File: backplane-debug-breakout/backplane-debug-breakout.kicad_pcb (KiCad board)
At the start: 2 copper layers, 65 x 50.5 mm, 11 parts, among them J1 Conn_02x08_Odd_Even, J2 Conn_01x04, J3 Conn_01x01_Socket, J4 Conn_01x01_Socket, J5 Conn_01x04, SW2 SW_Omron_B3FS, SW3 EG1218, U1 UMFT234XF

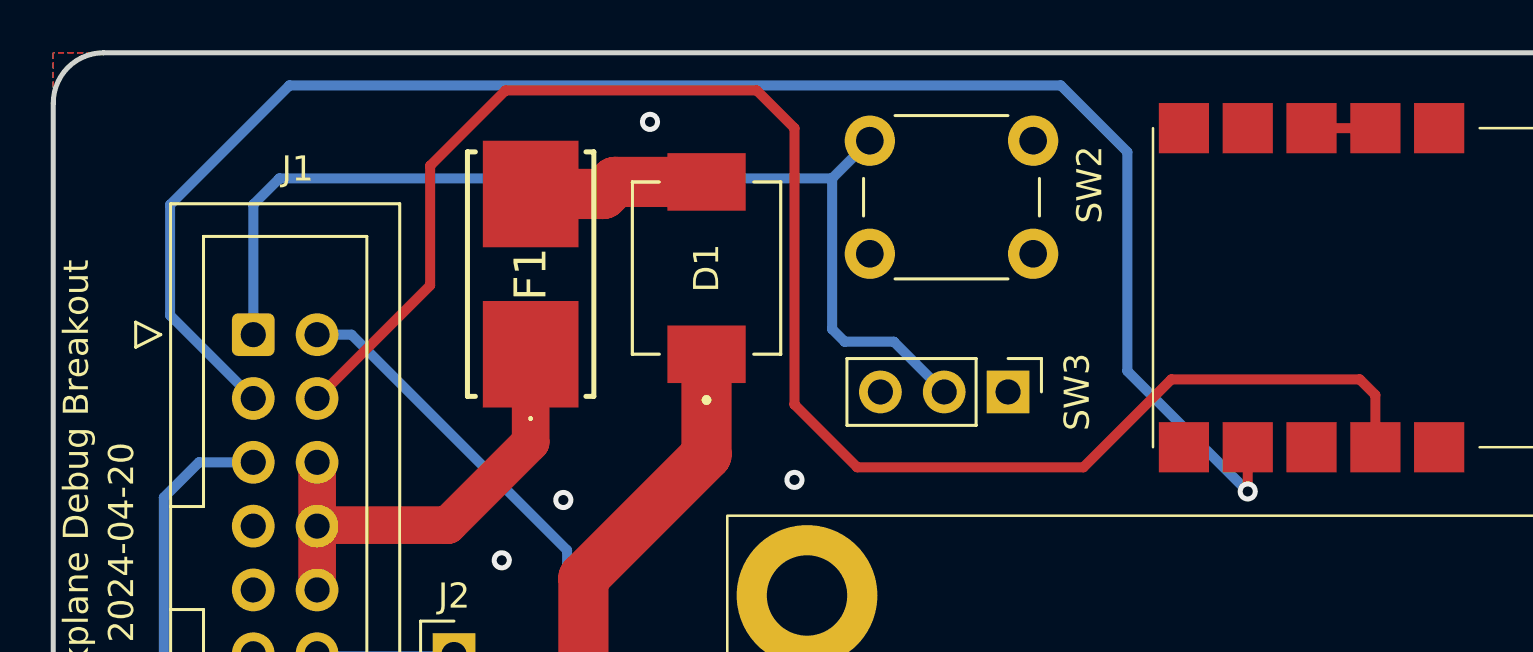
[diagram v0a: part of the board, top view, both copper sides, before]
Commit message: fixed tx-rx connections
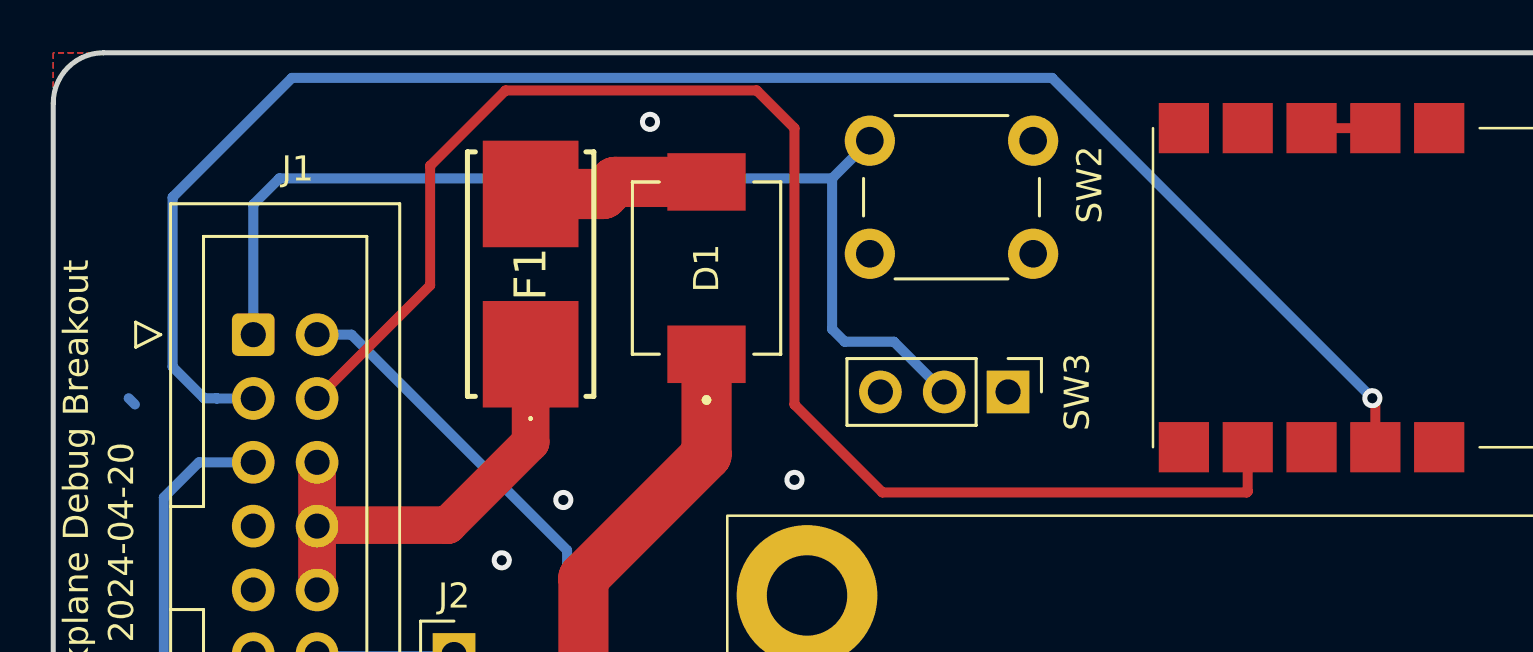
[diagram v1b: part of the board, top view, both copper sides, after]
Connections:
- U1 pad P7: /C3-UART-TX -> /C3-UART-RX
- U1 pad P9: /C3-UART-RX -> /C3-UART-TX
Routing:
- net /C3-UART-RX: track 66.4 -> 59.8 mm
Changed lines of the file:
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@@
 			)
 		)
-		(attr exclude_from_pos_files exclude_from_bom)
+		(attr exclude_from_pos_files exclude_from_bom allow_missing_courtyard)
 		(fp_rect
 			(start -3.175 -3.175)
@@
 			(size 2 2)
 			(layers "F.Cu" "F.Paste" "F.Mask")
-			(net 5 "/C3-UART-TX")
+			(net 8 "/C3-UART-RX")
 			(pinfunction "TXD")
 			(pintype "output")
@@
 			(size 2 2)
 			(layers "F.Cu" "F.Paste" "F.Mask")
-			(net 8 "/C3-UART-RX")
+			(net 5 "/C3-UART-TX")
 			(pinfunction "RXD")
 			(pintype "input")
@@
 			)
 		)
-		(property "Description" "16-position cable assembly socket"
+		(property "Description" "CONN HEADER VERT 16POS 2.54MM Y - 0"
 			(at 0 0 0)
 			(unlocked yes)
@@
 			)
 		)
-		(property "DPN" "H3DDH-1611618G-ND"
+		(property "DPN" "732-2095-ND"
 			(at 0 0 0)
 			(unlocked yes)
@@
 			)
 		)
-		(property "MPN" "H3DDH-161618G"
+		(property "MPN" "61201621621"
 			(at 0 0 0)
 			(unlocked yes)
@@
 			)
 		)
-		(property "MFR" "Assman"
+		(property "MFR" "Würth Elektronik"
 			(at 0 0 0)
 			(unlocked yes)
@@
 	)
 	(segment
-		(start 144.54 74.7)
-		(end 144.54 76.46)
+		(start 149.62 74.7)
+		(end 149.62 72.87)
 		(width 0.4)
 		(layer "F.Cu")
 		(net 5)
 	)
+	(segment
+		(start 149.62 72.87)
+		(end 149.5 72.75)
+		(width 0.4)
+		(layer "F.Cu")
+		(net 5)
+	)
 	(via
-		(at 144.54 76.46)
+		(at 149.5 72.75)
 		(size 0.8)
 		(drill 0.4)
@@
 	)
 	(segment
-		(start 139.75 62.95)
-		(end 137.1 60.3)
+		(start 101.75 71.5)
+		(end 103 72.75)
 		(width 0.4)
 		(layer "B.Cu")
@@
 	)
 	(segment
-		(start 144.54 76.46)
-		(end 139.75 71.67)
+		(start 103 72.75)
+		(end 103.5 72.75)
 		(width 0.4)
 		(layer "B.Cu")
@@
 	)
 	(segment
-		(start 139.75 71.67)
-		(end 139.75 62.95)
+		(start 101.75 64.75)
+		(end 101.75 71.5)
 		(width 0.4)
 		(layer "B.Cu")
@@
 	)
 	(segment
-		(start 101.65 65.05)
-		(end 101.65 69.45)
+		(start 136.75 60)
+		(end 106.5 60)
 		(width 0.4)
 		(layer "B.Cu")
@@
 	)
 	(segment
-		(start 101.65 69.45)
+		(start 100 72.75)
+		(end 100.25 73)
+		(width 0.4)
+		(layer "B.Cu")
+		(net 5)
+	)
+	(segment
+		(start 103.51 72.76)
 		(end 104.96 72.76)
 		(width 0.4)
@@
 	)
 	(segment
-		(start 106.4 60.3)
-		(end 101.65 65.05)
+		(start 106.5 60)
+		(end 101.75 64.75)
 		(width 0.4)
 		(layer "B.Cu")
@@
 	)
 	(segment
-		(start 137.1 60.3)
-		(end 106.4 60.3)
+		(start 103.5 72.75)
+		(end 103.51 72.76)
+		(width 0.4)
+		(layer "B.Cu")
+		(net 5)
+	)
+	(segment
+		(start 149.5 72.75)
+		(end 136.75 60)
 		(width 0.4)
 		(layer "B.Cu")
@@
 	)
 	(segment
-		(start 149.62 74.7)
-		(end 149.62 72.62)
+		(start 144.5 76.5)
+		(end 130 76.5)
 		(width 0.4)
 		(layer "F.Cu")
@@
 	)
 	(segment
-		(start 149 72)
-		(end 141.5 72)
+		(start 144.54 76.46)
+		(end 144.5 76.5)
 		(width 0.4)
 		(layer "F.Cu")
@@
 	)
 	(segment
-		(start 129 75.5)
+		(start 130 76.5)
 		(end 126.5 73)
+		(width 0.4)
+		(layer "F.Cu")
+		(net 8)
+	)
+	(segment
+		(start 112 68.26)
+		(end 107.5 72.76)
 		(width 0.4)
 		(layer "F.Cu")
@@
 	)
 	(segment
+		(start 125 60.5)
+		(end 115 60.5)
+		(width 0.4)
+		(layer "F.Cu")
+		(net 8)
+	)
+	(segment
+		(start 115 60.5)
+		(end 112 63.5)
+		(width 0.4)
+		(layer "F.Cu")
+		(net 8)
+	)
+	(segment
+		(start 144.54 74.7)
+		(end 144.54 76.46)
+		(width 0.4)
+		(layer "F.Cu")
+		(net 8)
+	)
+	(segment
 		(start 126.5 62)
 		(end 125 60.5)
 		(width 0.4)
 		(layer "F.Cu")
-		(net 8)
-	)
-	(segment
-		(start 115 60.5)
-		(end 112 63.5)
-		(width 0.4)
-		(layer "F.Cu")
-		(net 8)
-	)
-	(segment
-		(start 149.62 72.62)
-		(end 149 72)
-		(width 0.4)
-		(layer "F.Cu")
-		(net 8)
-	)
-	(segment
-		(start 125 60.5)
-		(end 115 60.5)
-		(width 0.4)
-		(layer "F.Cu")
-		(net 8)
-	)
-	(segment
-		(start 138 75.5)
-		(end 129 75.5)
-		(width 0.4)
-		(layer "F.Cu")
-		(net 8)
-	)
-	(segment
-		(start 112 68.26)
-		(end 107.5 72.76)
-		(width 0.4)
-		(layer "F.Cu")
-		(net 8)
-	)
-	(segment
-		(start 141.5 72)
-		(end 138 75.5)
-		(width 0.4)
-		(layer "F.Cu")

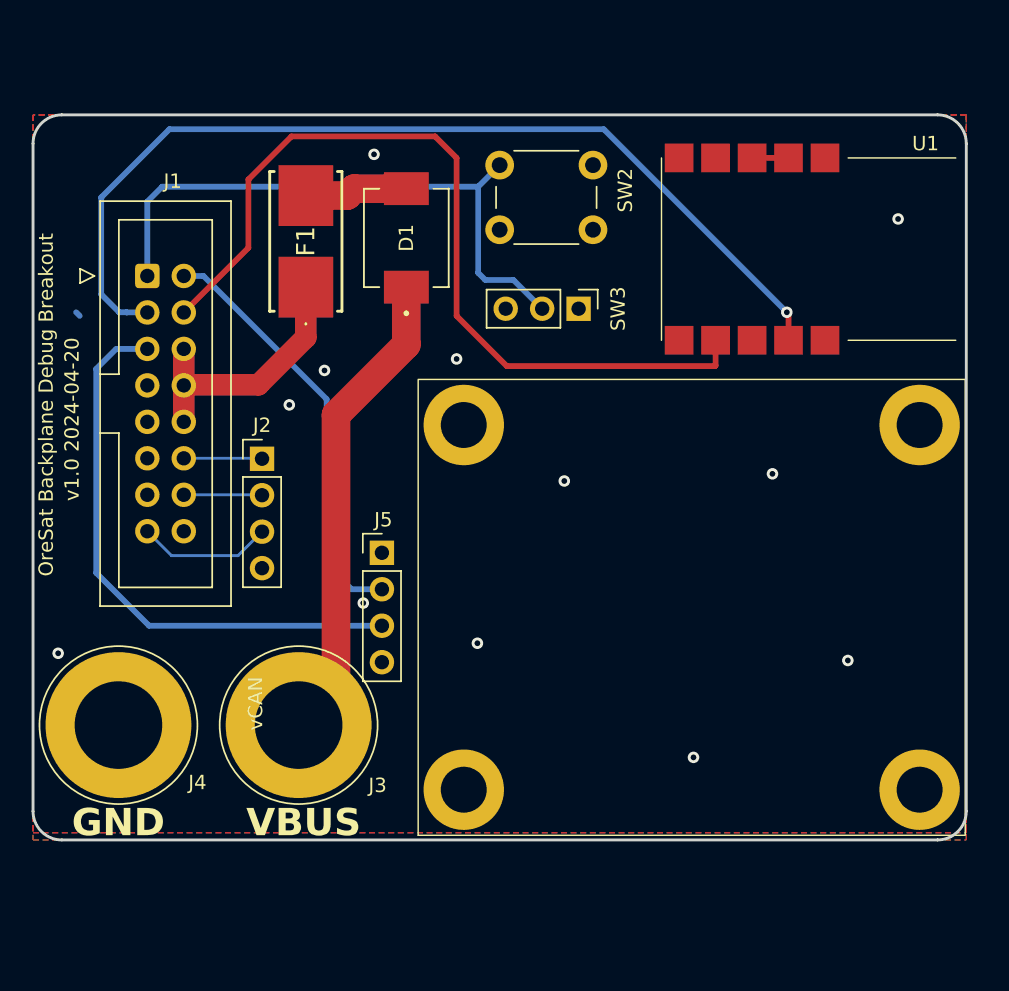
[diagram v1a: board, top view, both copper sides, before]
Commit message: added usb-serial connector to schematic and pcb
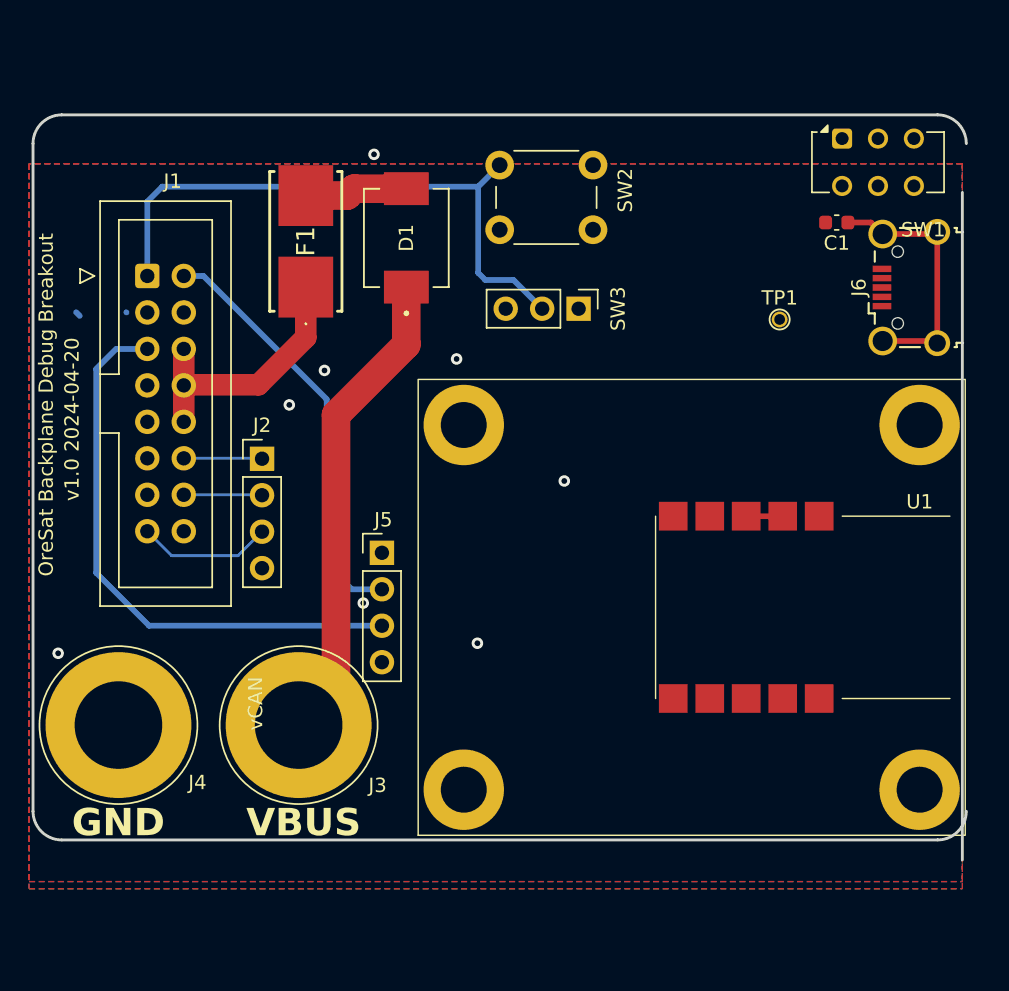
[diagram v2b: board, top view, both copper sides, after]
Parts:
- added C1: 100n, Capacitor_SMD:C_0603_1608Metric, F.Cu at (153.0, 66.5)
- added J6: 629105150521, Connector_USB:USB_Micro-B_Wuerth_629105150521_CircularHoles, F.Cu at (158.0, 71.0)
- added SW1: SW_Push_DPDT, oresat-passives:DPDT slide switch 6 pin, F.Cu at (159.0, 67.5)
- added TP1: TestPoint, oresat-misc:TestPoint-0.75mm-th, F.Cu at (149.0, 73.2)
- moved U1 25.0 mm to (161.4, 87.0)
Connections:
- U1 pad P7: /C3-UART-RX -> Net-(U1-TXD)
- U1 pad P9: /C3-UART-TX -> Net-(U1-RXD)
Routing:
- net /C3-UART-TX: track 67.8 -> 0.37 mm, vias 1 -> 0
- net /C3-UART-RX: track 59.8 -> 0.00 mm
- net Net-(J6-Shield): track 0.00 -> 18.4 mm
- net GND: vias 12 -> 8
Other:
- board size 65 x 50.5 mm -> 65 x 51.9 mm

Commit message: made changes to layout of pcb
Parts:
- removed J3: Conn_01x01_Socket, Connector:Banana_Jack_1Pin
- J4: value Conn_01x01_Socket -> Conn_01x02_Socket; footprint Connector:Banana_Jack_1Pin -> oresat-connectors:PHOENIX_1995499
- moved SW3 16.5 mm to (122.3, 62.0)
- moved F1 14.3 mm to (130.3, 67.6)
- moved D1 13.8 mm to (136.8, 67.6)
- moved SW2 13.5 mm to (123.0, 70.8)
- moved SW1 9.85 mm to (149.3, 69.2)
- moved J4 9.15 mm to (97.0, 94.5)
- moved TP1 4.50 mm to (152.4, 70.3)
- moved J6 3.15 mm to (158.1, 67.9)
- moved U1 2.71 mm to (161.1, 84.2)
- moved vCAN 2.71 mm to (126.8, 103.3)
- moved C1 2.40 mm to (152.9, 64.1)
- moved J2 2.30 mm to (115.0, 81.9)
- moved J1 1.78 mm to (106.7, 70.6)
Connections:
- J4 pad 1: GND -> Net-(D1-A)
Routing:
- net /C3-UART-TX: track 0.37 -> 53.2 mm
- net Net-(U1-RXD): track 0.26 -> 49.2 mm
- net /C3-UART-RX: track 0.00 -> 42.9 mm, vias 0 -> 1
- net Net-(U1-TXD): track 0.00 -> 35.0 mm
- net /SD: track 42.3 -> 25.2 mm
- net Net-(J6-D-): track 0.00 -> 11.5 mm
- net /VBUS: track 18.5 -> 29.2 mm
- net Net-(D1-A): track 34.3 -> 44.2 mm
- net Net-(J6-D+): track 0.00 -> 9.10 mm, vias 0 -> 2
- net Net-(J6-VBUS): track 0.00 -> 4.22 mm
- net /CAN_L: track 29.6 -> 27.7 mm
- net /CAN_H: track 39.8 -> 38.1 mm
- net /OPD_SCL: track 9.87 -> 11.5 mm
- net /OPD_PWR: track 5.46 -> 6.35 mm
- net /OPD_SDA: track 5.46 -> 6.34 mm
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- added copper zone on B.Cu, net Net-(D1-A)
- added copper zone on F.Cu, net Net-(D1-A)
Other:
- board size 65 x 51.9 mm -> 65 x 60.5 mm
- board text removed: "GND"
- board text removed: "VBUS"

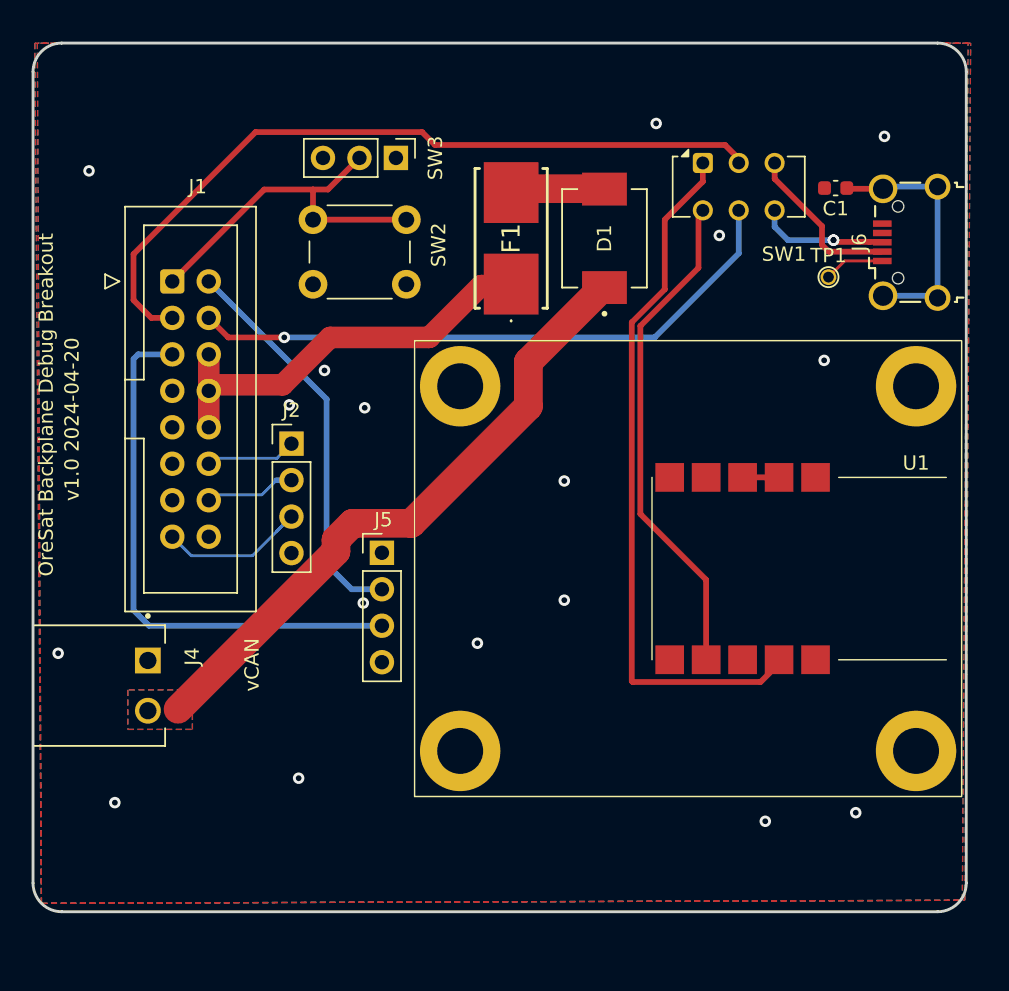
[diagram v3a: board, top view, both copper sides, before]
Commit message: added LED to schematic and modified pcb
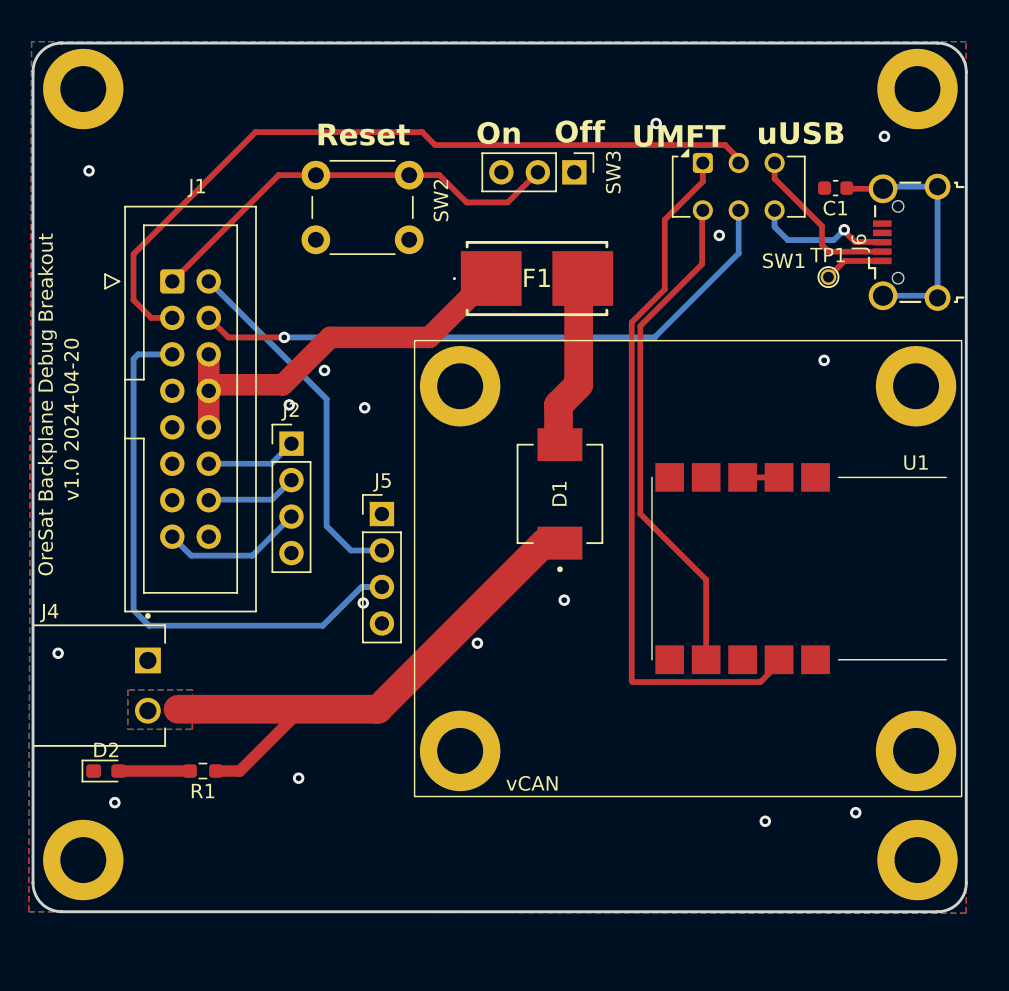
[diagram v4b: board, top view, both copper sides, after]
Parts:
- added ?: , , F.Cu at (100.5, 110.9)
- added ?: , , F.Cu at (158.6, 110.9)
- added ?: , , F.Cu at (100.5, 57.2)
- added ?: , , F.Cu at (158.6, 57.2)
- added D2: LED, LED_SMD:LED_0603_1608Metric_Pad1.05x0.95mm_HandSolder, F.Cu at (102.1, 104.7)
- added R1: R_US, Resistor_SMD:R_0603_1608Metric_Pad0.98x0.95mm_HandSolder, F.Cu at (108.8, 104.7)
- moved D1 18.1 mm to (133.7, 85.4)
- moved SW3 12.5 mm to (134.7, 63.0)
- moved F1 3.33 mm to (132.1, 70.4), turned to 0 degrees
- moved SW2 3.11 mm to (123.2, 67.7)
- moved J5 2.70 mm to (121.3, 86.8)
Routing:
- net Net-(D1-K): track 6.62 -> 14.6 mm
- net Net-(D1-A): track 44.2 -> 39.1 mm
- net /SD: track 25.2 -> 30.2 mm
- net Net-(D2-A): track 0.00 -> 4.95 mm
- net /CAN_L: track 27.7 -> 25.0 mm
- net /OPD_SCL: track 11.5 -> 9.97 mm
- net /VBUS: track 29.2 -> 28.0 mm
- net /CAN_H: track 38.1 -> 39.2 mm
- net Net-(J6-D+): track 9.10 -> 9.70 mm, vias 2 -> 1
- net GND: vias 17 -> 16
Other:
- board text added: "Off"
- board text added: "On"
- board text added: "Reset"
- board text added: "UMFT"
- board text added: "uUSB"

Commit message: finished
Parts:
- added REF**: logo-small, oresat-graphics:logo-small, F.Cu at (110.6, 109.9)
- moved D2 36.7 mm to (117.8, 71.5)
- moved R1 35.7 mm to (122.1, 71.5)
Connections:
- R1 pad 1: Net-(D1-A) -> /VBUS
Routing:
- net Net-(D1-A): track 39.1 -> 31.4 mm
- net Net-(D2-A): track 4.95 -> 0.00 mm
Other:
- board text added: "Temp"
- board text added: "UART"
- board text added: "USB"
- board text added: "~{Shutdown}"
- board text removed: "Reset"
- board text removed: "UMFT"
- board text removed: "uUSB"

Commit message: updated BOM
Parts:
- U1: footprint oresat-misc:UMFT234XF -> oresat-pcbs:UMFT234XF
- moved TP1 1.23 mm to (152.0, 69.2)
- moved D2 0.85 mm to (117.0, 71.5)
- moved R1 0.85 mm to (121.2, 71.5)
- moved D1 0.75 mm to (133.7, 84.7)
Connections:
- J4 pad 1: Net-(D1-A) -> GND
- J4 pad 2: GND -> Net-(D1-A)
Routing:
- net Net-(D2-A): track 0.00 -> 2.48 mm
- net /VBUS: track 28.4 -> 30.6 mm
- net Net-(D1-A): track 31.4 -> 32.8 mm
- net Net-(J6-D+): track 9.70 -> 8.52 mm
- net Net-(D1-K): track 14.6 -> 13.8 mm
- net Net-(J6-D-): track 11.5 -> 10.7 mm
- net /C3-UART-TX: track 53.2 -> 52.4 mm
- net GND: vias 16 -> 34
